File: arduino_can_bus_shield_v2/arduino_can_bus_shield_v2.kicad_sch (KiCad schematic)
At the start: 25 parts

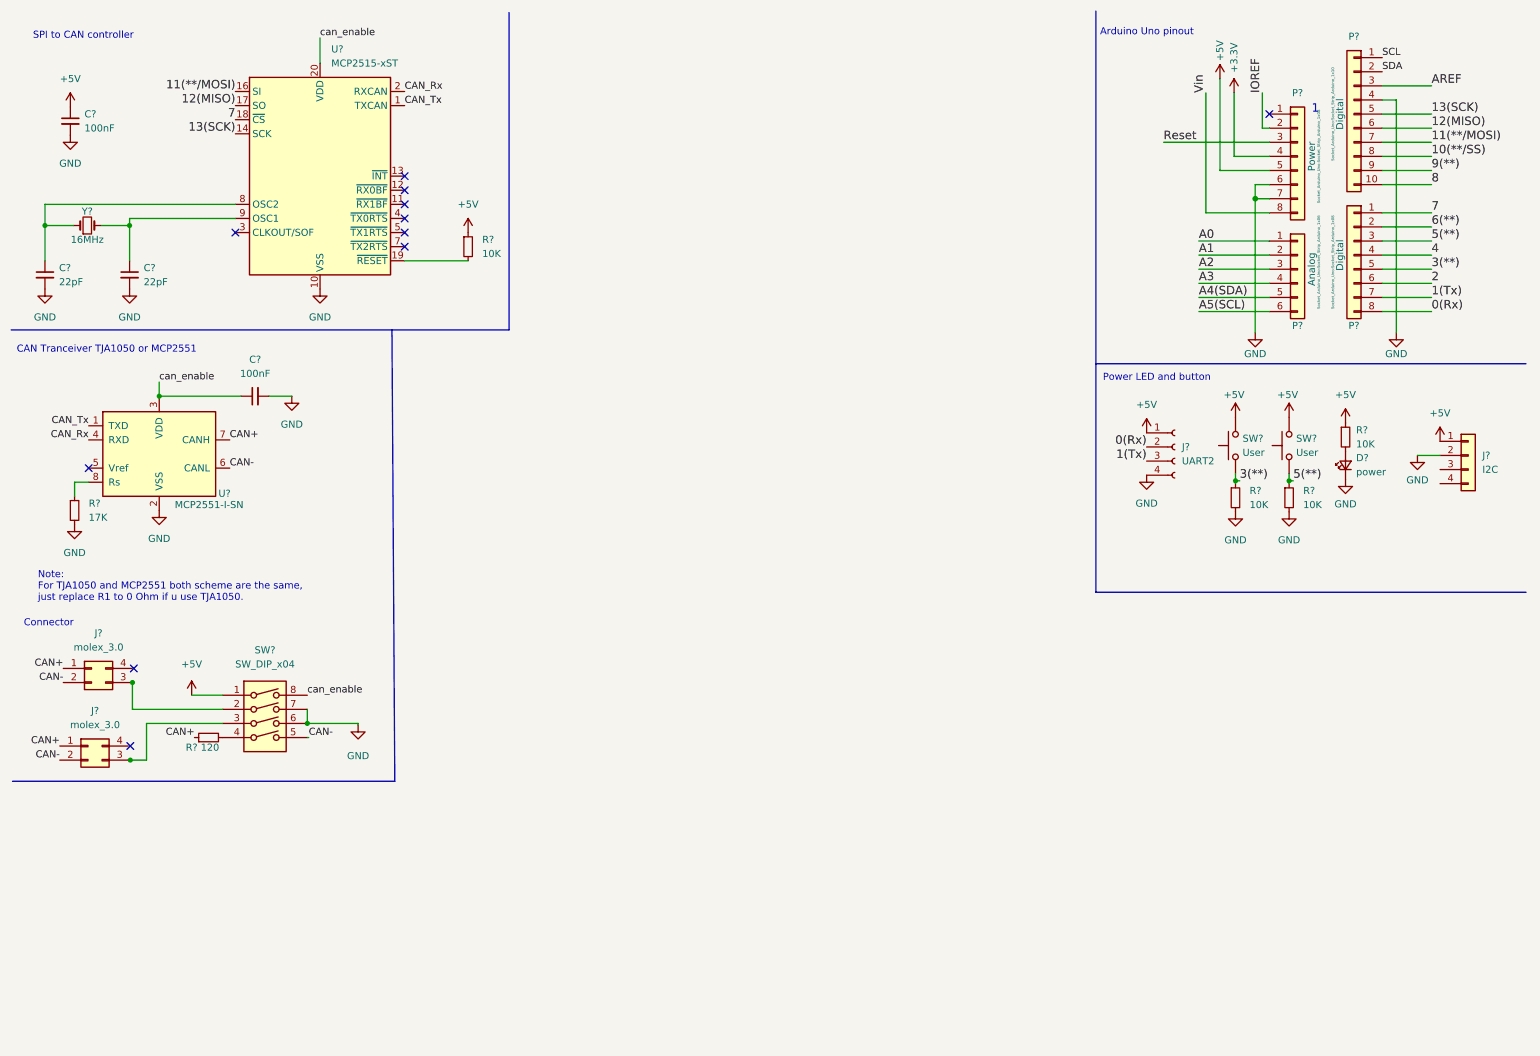
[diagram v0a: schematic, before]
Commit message: new arduio shield
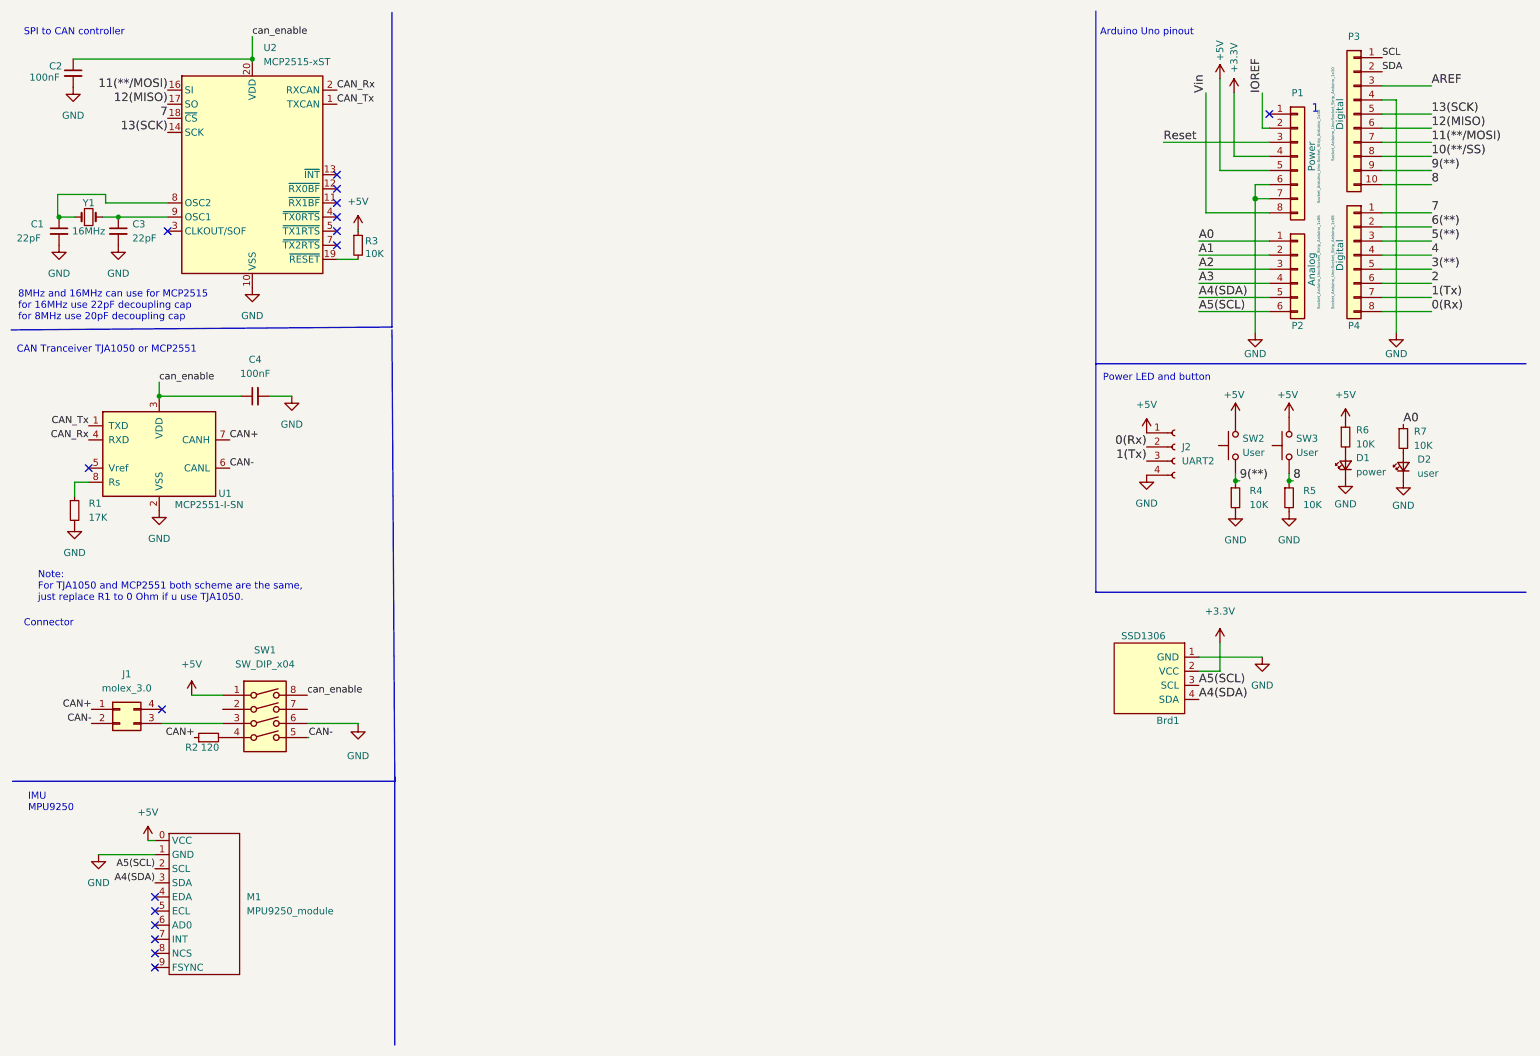
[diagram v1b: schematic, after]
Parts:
- removed J?: I2C, symbol Connector_Generic:Conn_01x04
- removed J?: molex_3.0, Connector_Molex:Molex_Micro-Fit_3.0_43045-0400_2x02_P3.00mm_Horizontal, symbol Connector_Generic:Conn_02x02_Counter_Clockwise
- added Brd1: SSD1306, PolyuRobotics:128x64OLED, symbol PolyuRobotics:SSD1306
- added D2: user, LED_SMD:LED_0805_2012Metric_Pad1.15x1.40mm_HandSolder, symbol Device:LED_Small
- added M1: MPU9250_module, PolyuRobotics:MPU9250_module, symbol PolyuRobotics:MPU9250_module
- added R7: 10K, Resistor_SMD:R_0805_2012Metric_Pad1.20x1.40mm_HandSolder, symbol Device:R_Small
- gave numbers to parts that had none: 23
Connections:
- net +5V: now also M1.0 (VCC); no longer C2.1
- net 3(**): no longer R4.1, SW2.1
- net 5(**): no longer R5.1, SW3.1
- net 8: now also R5.1, SW3.1
- net 9(**): now also R4.1, SW2.1
- net A0: now also R7.1
- net A4(SDA): now also Brd1.4 (SDA), M1.3 (SDA)
- net A5(SCL): now also Brd1.3 (SCL), M1.2 (SCL)
- net GND: now also Brd1.1 (GND), D2.1 (K), M1.1 (GND); no longer SW1.7
- net can_enable: now also C2.1
- new net: D2.2 (A), R7.2
- new net +3.3V: Brd1.2 (VCC)
- no-connect marks 11 -> 16
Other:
- note added: "8MHz and 16MHz can use for MCP2515 for 16MHz use 22pF decoupling cap for 8MHz use 20pF decoupling cap"
- note added: "IMU MPU9250"
- moved on the sheet: C1, C2, C3, J1, R3, U2, Y1
